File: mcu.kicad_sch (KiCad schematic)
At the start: 18 parts, among them SW19 EVQQ2, SW8 EVQQ2, U9 STM32F405RGTx, Y1 8MHz

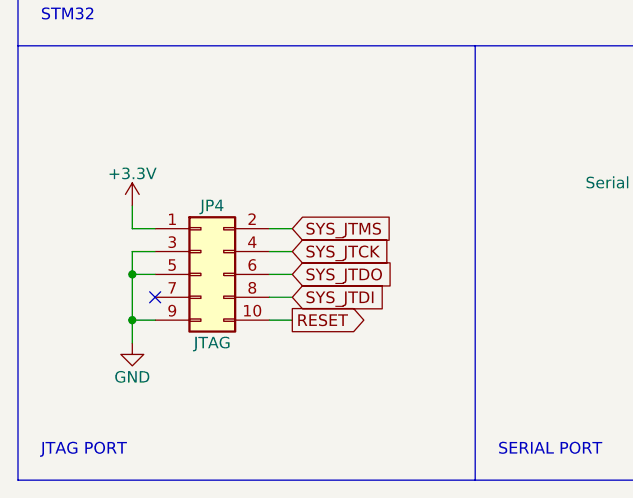
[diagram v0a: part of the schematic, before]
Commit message: Changed mini-JTAG to SWD
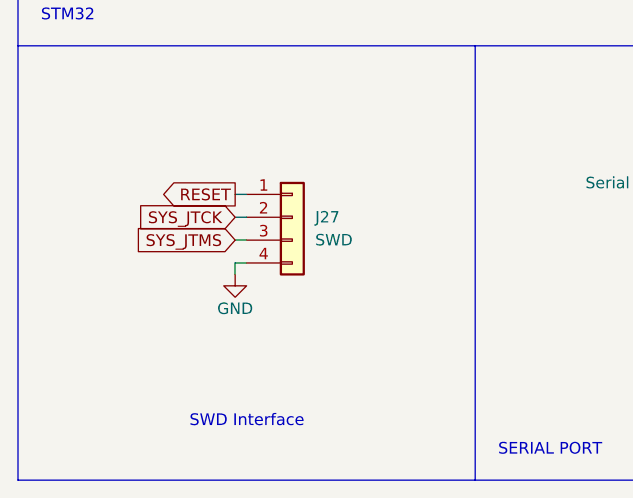
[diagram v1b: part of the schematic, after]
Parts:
- removed JP4: JTAG, Connector_PinHeader_1.27mm:PinHeader_2x05_P1.27mm_Vertical, symbol Connector_Generic:Conn_02x05_Odd_Even
- added J27: SWD, Connector_PinHeader_2.54mm:PinHeader_1x04_P2.54mm_Vertical, symbol Connector_Generic:Conn_01x04
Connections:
- net GND: now also J27.4 (Pin_4)
- net RESET: now also J27.1 (Pin_1)
- net SYS_JTCK: now also J27.2 (Pin_2)
- net SYS_JTMS: now also J27.3 (Pin_3)
- no-connect marks 13 -> 12
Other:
- note added: "SWD Interface"
- note removed: "JTAG PORT"

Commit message: v1.1
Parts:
- renumbered J27 to JP4
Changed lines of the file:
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@@
     (title "PER|FORMER eurorack sequencer")
     (date "2018-10-09")
-    (rev "1.0")
+    (rev "1.1")
     (company "westlicht")
     (comment 1 "cc-by-nc-sa")
@@
   (symbol (lib_id "Connector_Generic:Conn_01x04") (at 45.72 166.37 0) (unit 1)
     (in_bom yes) (on_board yes) (fields_autoplaced)
-    (property "Reference" "J27" (id 0) (at 48.26 166.3699 0)
-      (effects (font (size 1.27 1.27)) (justify left))
-    )
+    (property "Reference" "JP4" (id 0) (at 48.26 166.3699 0)
+      (effects (font (size 1.27 1.27)) (justify left))
+    )
